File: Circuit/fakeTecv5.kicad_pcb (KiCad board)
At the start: 2 copper layers, 25.4 x 52.1 mm, 78 parts, among them J1 EXTRA, J11 FET1 3,3, J12 FET2 3,3, J13 FET3 3,3, J14 GPS Pins, J16 Encoder Pads, J37 SCL, J38 JST-SH-4, J39 SDA, J40 3.3V, J41 GND, J42 FET1, J43 FET2, J44 FET3, J45 GND, J46 3.3V, J47 GND, J48 GND, J49 GND, J5 I2C Oled screen, J50 3.3V, J51 GND, J52 GND, J6 FET1 Drain, J7 FET2 Drain, J8 FET3 Drain, J9 JST-PH-2, Q1 AO3400A, Q2 AO3400A, Q3 AO3400A, SW1 Reset, SW2 SW_Push, U1 XB8089D0, U2 HT-RA62, U3 nice!nano v2

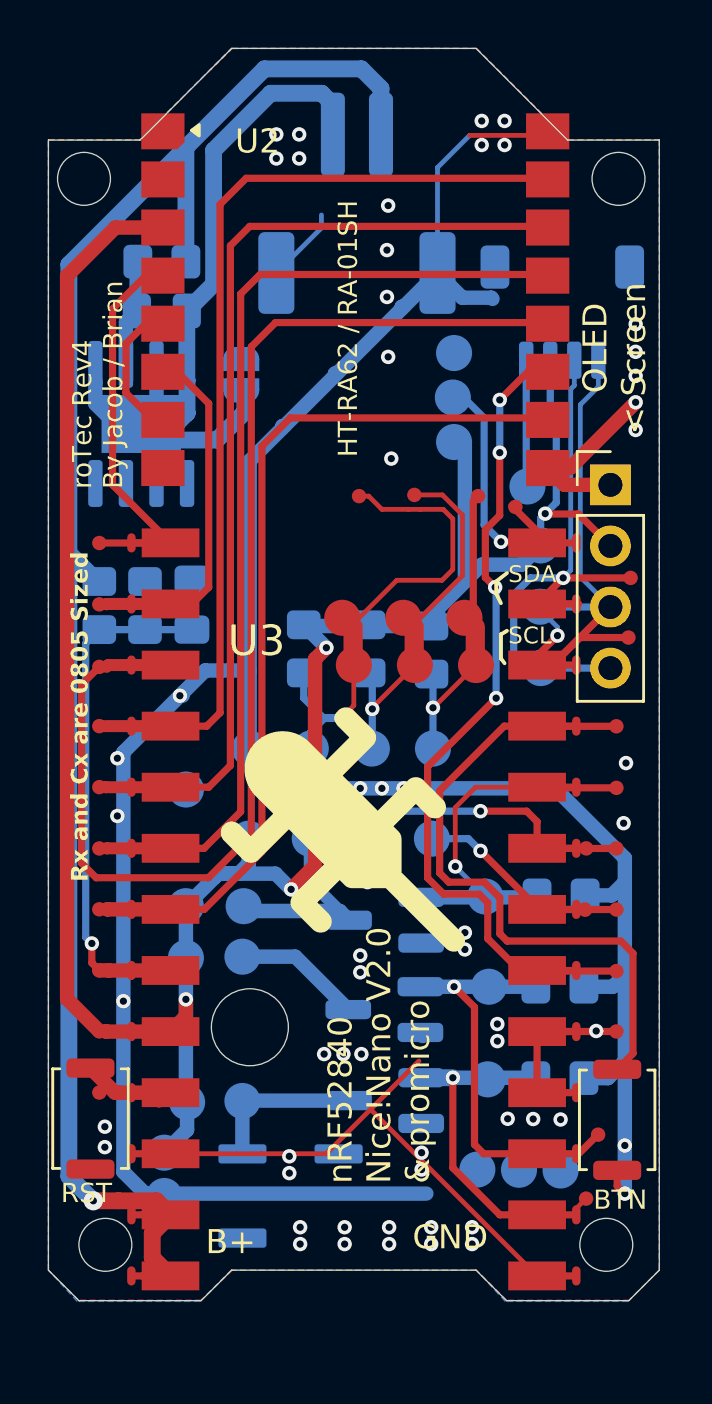
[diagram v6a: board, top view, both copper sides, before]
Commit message: rotate small i2c connector
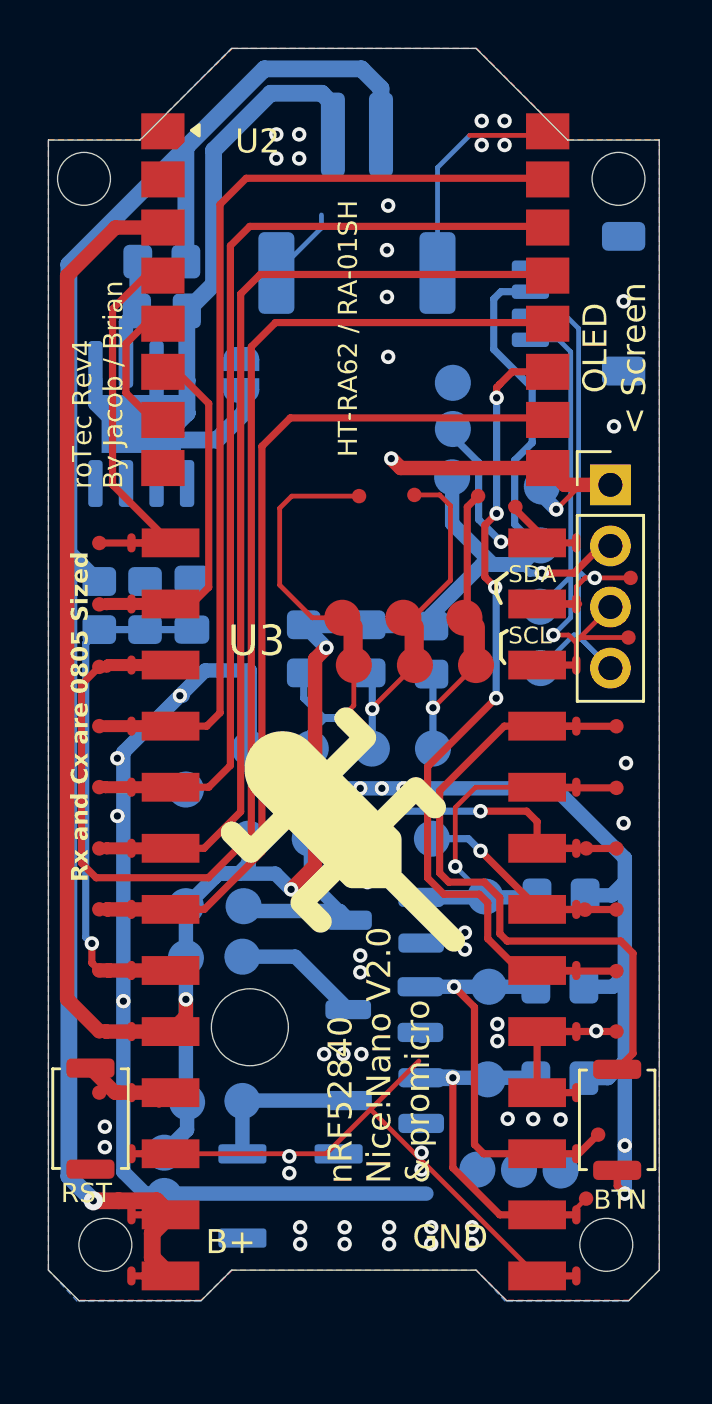
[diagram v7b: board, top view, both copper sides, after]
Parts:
- moved J46 1.47 mm to (115.7, 44.8)
- moved J1 1.31 mm to (115.7, 42.8)
- moved J45 1.24 mm to (115.7, 40.9)
- moved J38 0.76 mm to (120.9, 37.6), turned to -90 degrees
- moved J41 0.60 mm to (119.4, 45.2)
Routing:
- net GND: track 154.5 -> 133.1 mm, vias 60 -> 58
- net +3.3V: track 103.4 -> 107.9 mm
- net /ENC_PUSH: track 20.7 -> 17.4 mm
- net /SCL: track 25.2 -> 23.1 mm
- net /SDA: track 25.4 -> 26.9 mm
- net /EXTRA: track 9.20 -> 7.84 mm
- net /RXEN: track 34.3 -> 34.8 mm
